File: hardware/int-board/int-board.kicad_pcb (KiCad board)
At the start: 2 copper layers, 59 x 85 mm, 25 parts, among them J1 PTSM 0,5/4-HH-2,5-THR, J2 PTSM 0,5/4-HH-2,5-THR, J3 PTSM 0,5/4-HH-2,5-THR, J4 PTSM 0,5/4-HH-2,5-THR, J5 Pi 40-pin socket, J6 GH SM07B link to EXT, J9 GPIO breakout, U1 LTV-847, U2 LTV-847, U3 LTV-847

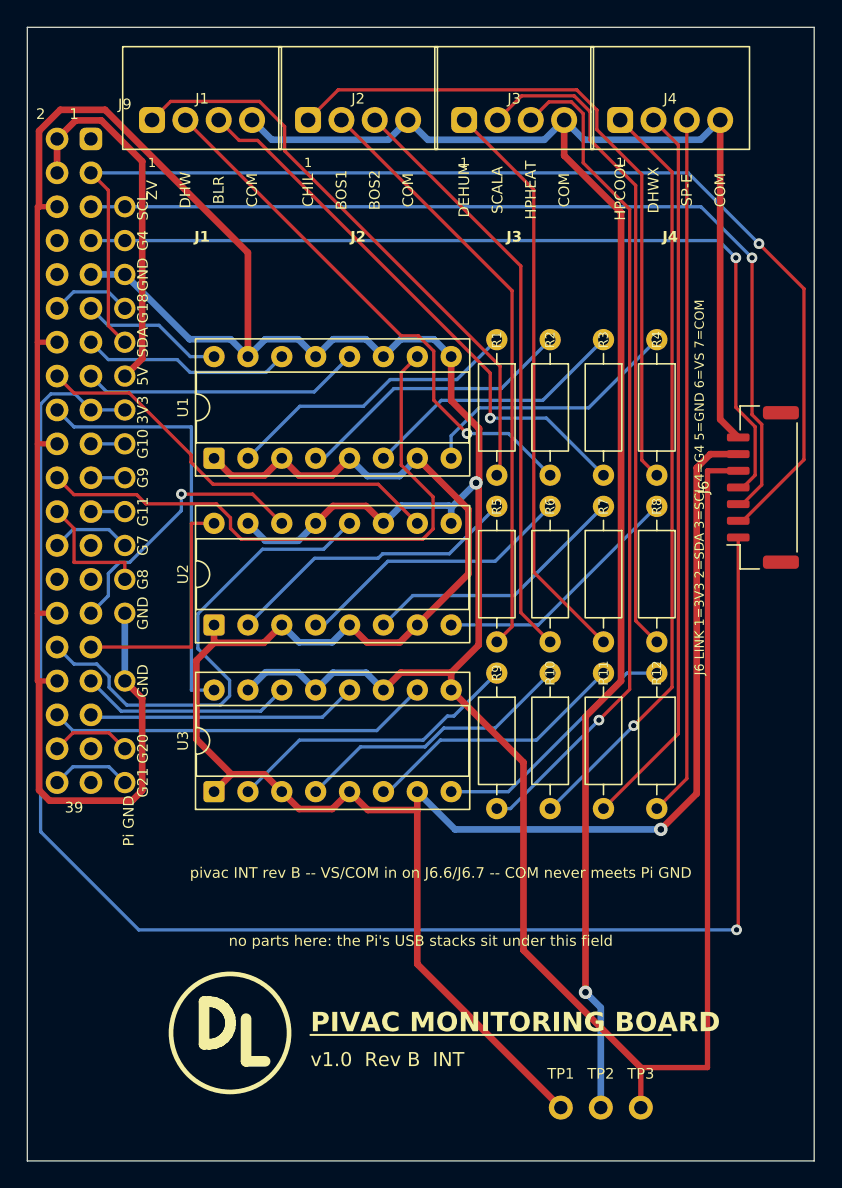
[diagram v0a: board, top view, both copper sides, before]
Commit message: Silkscreen: INT header pin numbers on their pins, J9 above its column, J5's back reference hidden; EXT probe-end labels aligned
Co-Authored-By: Claude Fable 5.1 <noreply@anthropic.com>
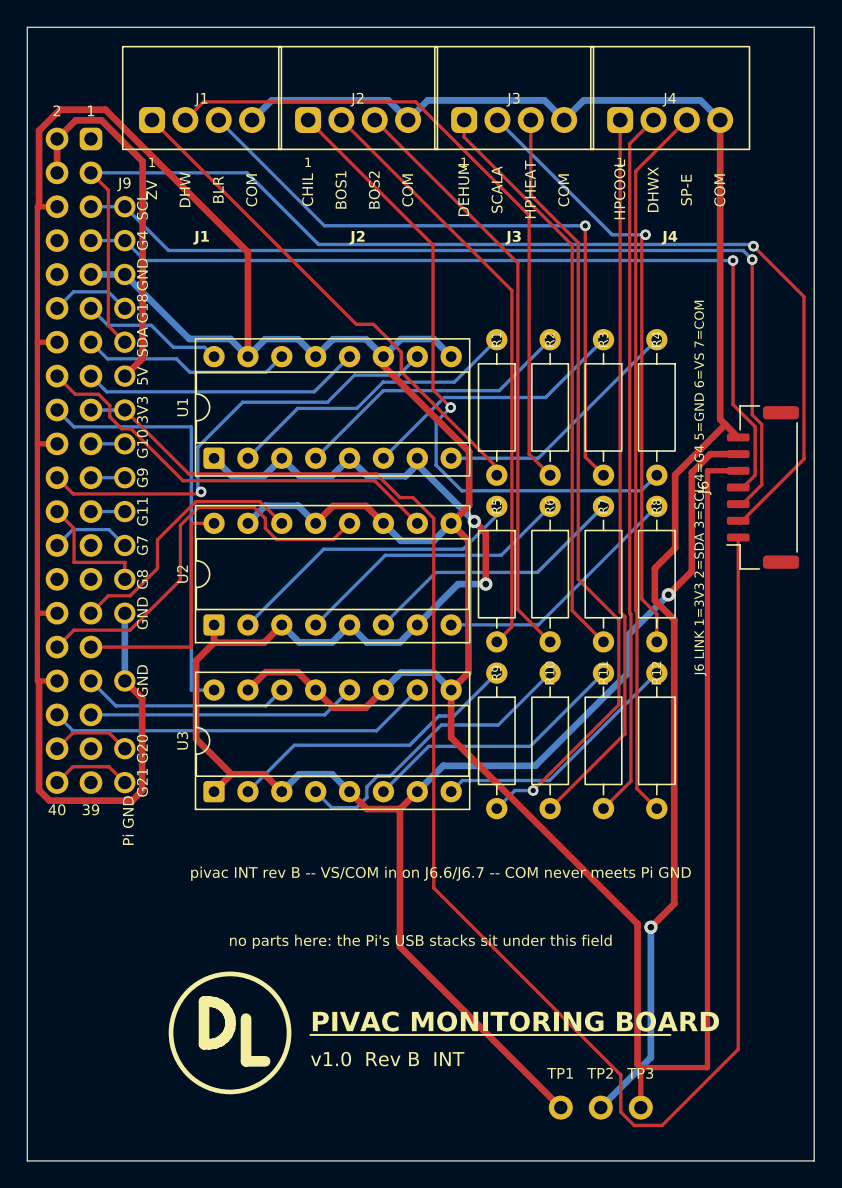
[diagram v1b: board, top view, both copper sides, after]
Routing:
- net COM: track 140.5 -> 119.4 mm
- net GPIO25: track 45.3 -> 34.1 mm, vias 0 -> 1
- net S_DHW: track 40.5 -> 50.0 mm, vias 1 -> 0
- net VS: track 162.3 -> 153.5 mm, vias 1 -> 3
- net S_BLR: track 41.9 -> 50.0 mm
- net GPIO12: track 36.8 -> 30.6 mm
- net S_ZV: track 44.2 -> 38.1 mm
- net 3V3: track 123.9 -> 129.4 mm, vias 1 -> 0
- net S_SCALA: track 50.0 -> 45.8 mm, vias 0 -> 1
- net S_HPHEAT: track 63.1 -> 59.0 mm
- net S_CHIL: track 52.5 -> 48.6 mm, vias 0 -> 1
- net S_HPCOOL: track 57.1 -> 54.1 mm, vias 1 -> 0
- net S_DHWX: track 54.7 -> 53.3 mm
- net K10: track 21.3 -> 22.7 mm
- net S_SP-E: track 52.6 -> 53.9 mm
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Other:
- board text added: "40"

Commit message: Silkscreen: J6 reference below the header, the trunk label beside H1's pin letters
Co-Authored-By: Claude Fable 5.1 <noreply@anthropic.com>
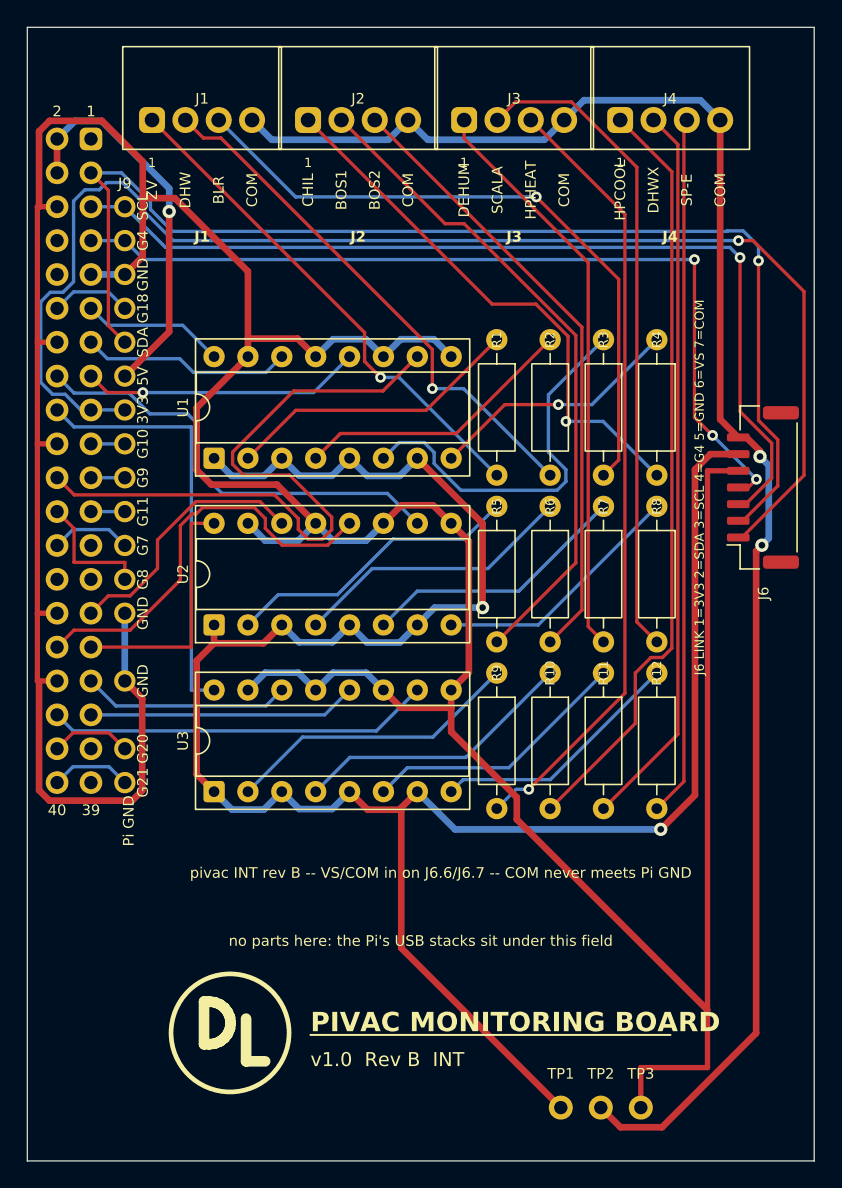
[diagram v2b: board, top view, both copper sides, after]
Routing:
- net 3V3: track 129.4 -> 102.1 mm, vias 0 -> 1
- net GPIO25: track 34.1 -> 51.0 mm, vias 1 -> 0
- net VS: track 153.5 -> 165.9 mm, vias 3 -> 2
- net S_DHW: track 50.0 -> 40.1 mm, vias 0 -> 1
- net K3: track 20.2 -> 29.3 mm
- net S_CHIL: track 48.6 -> 41.1 mm
- net COM: track 119.4 -> 124.7 mm, vias 1 -> 2
- net S_BOS1: track 44.9 -> 49.7 mm
- net GND: track 296.0 -> 292.2 mm
- net S_SCALA: track 45.8 -> 49.3 mm, vias 1 -> 0
- net S_HPCOOL: track 54.1 -> 57.5 mm
- net S_BOS2: track 44.6 -> 46.5 mm
- net +5V: track 27.5 -> 29.1 mm, vias 0 -> 1
- net GPIO23: track 32.1 -> 33.6 mm
- net K10: track 22.7 -> 21.3 mm
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
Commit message: EXT silkscreen: converter pins labelled one by one, R1's reference under R1, link legend beside J1
Co-Authored-By: Claude Fable 5.1 <noreply@anthropic.com>
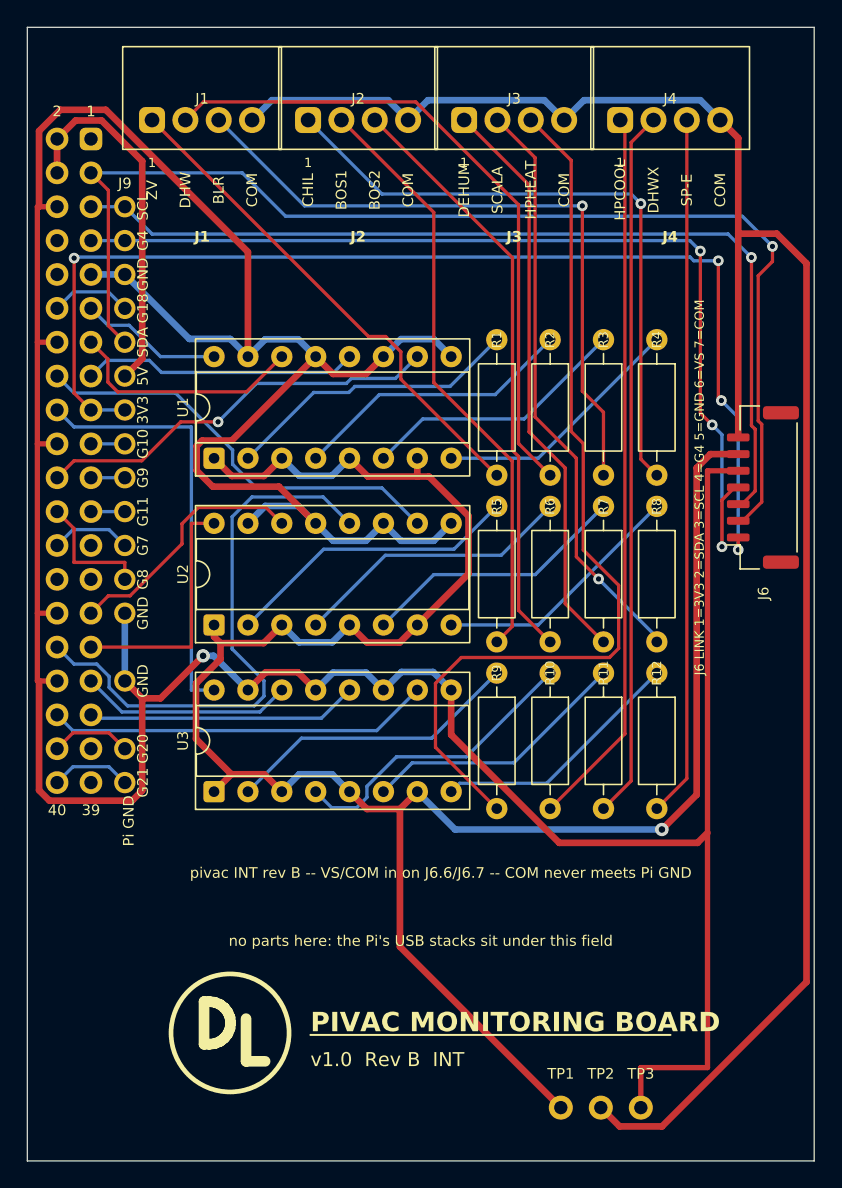
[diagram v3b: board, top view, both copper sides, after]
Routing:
- net GPIO25: track 51.0 -> 30.8 mm, vias 0 -> 1
- net COM: track 124.7 -> 143.6 mm, vias 2 -> 0
- net 3V3: track 102.1 -> 86.1 mm, vias 1 -> 4
- net GPIO12: track 30.9 -> 42.8 mm
- net S_DHW: track 40.1 -> 50.0 mm, vias 1 -> 0
- net S_HPHEAT: track 59.1 -> 68.5 mm, vias 1 -> 0
- net K3: track 29.3 -> 20.2 mm
- net GPIO4: track 65.9 -> 74.0 mm
- net S_CHIL: track 41.1 -> 48.4 mm
- net S_SCALA: track 49.3 -> 44.1 mm, vias 0 -> 1
- net S_BOS1: track 49.7 -> 44.9 mm
- net VS: track 165.9 -> 162.1 mm, vias 2 -> 1
- net S_HPCOOL: track 57.5 -> 54.1 mm
- net GPIO27: track 15.7 -> 18.0 mm
- net S_BOS2: track 46.5 -> 44.6 mm
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
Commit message: EXT silkscreen: R1 and F1 references moved clear, link legend in three lines beside J1
Co-Authored-By: Claude Fable 5.1 <noreply@anthropic.com>
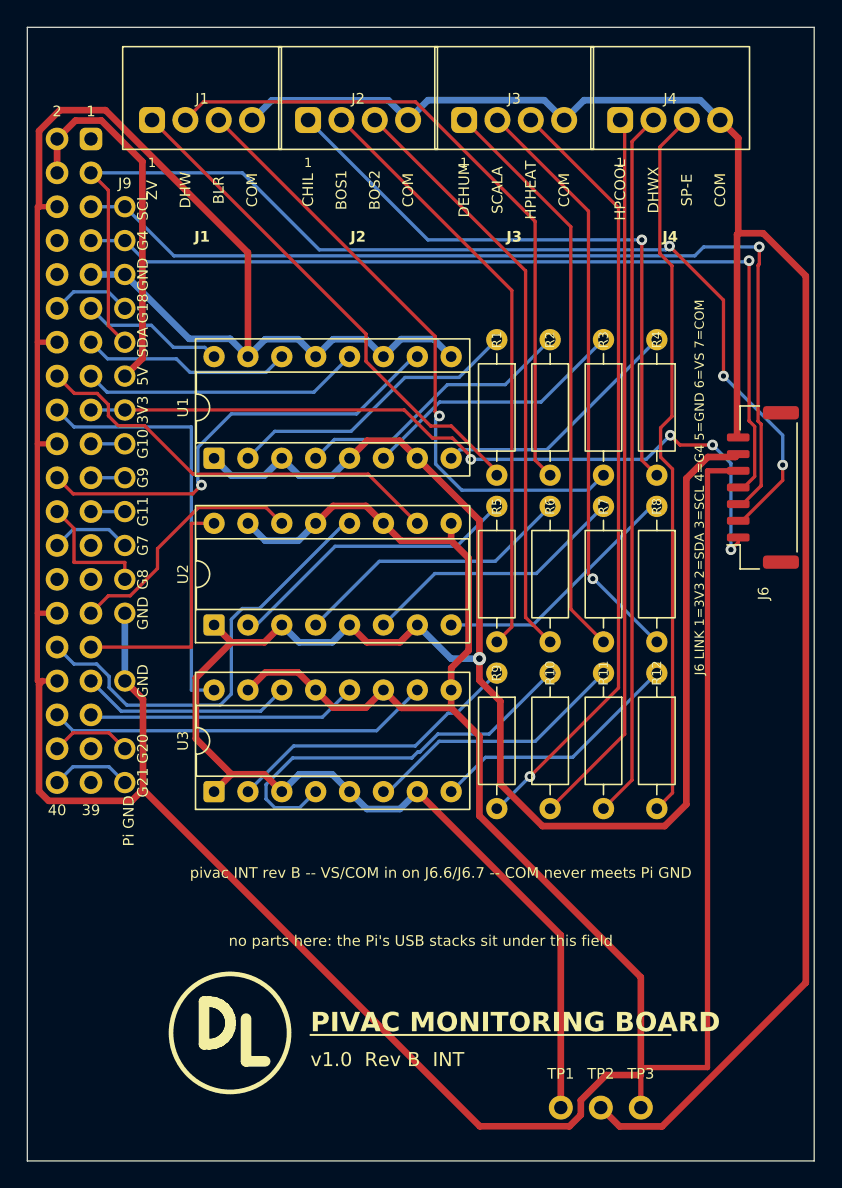
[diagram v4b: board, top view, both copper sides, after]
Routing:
- net GND: track 293.2 -> 329.4 mm, vias 1 -> 0
- net 3V3: track 86.1 -> 58.9 mm
- net VS: track 162.1 -> 173.4 mm
- net S_HPHEAT: track 68.5 -> 58.2 mm, vias 0 -> 1
- net GPIO12: track 42.8 -> 33.1 mm
- net K10: track 22.7 -> 30.3 mm
- net GPIO4: track 74.0 -> 68.0 mm, vias 3 -> 1
- net S_BLR: track 50.8 -> 46.6 mm
- net SDA: track 89.2 -> 85.3 mm, vias 1 -> 3
- net GPIO25: track 30.8 -> 33.8 mm
- net GPIO27: track 18.0 -> 15.7 mm
- net SCL: track 70.4 -> 72.2 mm
- net S_CHIL: track 48.4 -> 46.9 mm
- net S_SP-E: track 52.6 -> 54.1 mm
- net COM: track 143.6 -> 143.0 mm

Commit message: Rev B INT: 10 kΩ LED resistors in place of 12 kΩ
The resistor assortment on hand has 10 kΩ and 22 kΩ but no 12 kΩ. 10 kΩ
sets 3.4 mA per channel from the 35 V sense rail (0.11 W, under half the
1/4 W rating, far under the LTV-847's 50 mA), adds 7 mA to the bridge with
all twelve channels on, and keeps the relay contacts at a higher wetting
current. 22 kΩ would drop to about 1 mA at 21.6 VAC under the Pi's load,
half the current any build has proven.

The value appears in no gerber layer, so the ordered boards are unchanged;
the generated BOM, schematic and KiCad files are edited in place rather
than rebuilt, which would reroute the board. Rev A keeps its 12 kΩ.

Co-Authored-By: Claude Opus 5.5 <noreply@anthropic.com>
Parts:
- R1, R10, R11, R12, R2, R3, R4, R5, R6, R7, R8, R9: value 12k 1/4W -> 10k 1/4W
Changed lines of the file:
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@@
 			)
 		)
-		(property "Value" "12k 1/4W"
+		(property "Value" "10k 1/4W"
 			(at 5.08 2.37 270)
 			(layer "F.Fab")
@@
 			)
 		)
-		(property "Value" "12k 1/4W"
+		(property "Value" "10k 1/4W"
 			(at 5.08 2.37 270)
 			(layer "F.Fab")
@@
 			)
 		)
-		(property "Value" "12k 1/4W"
+		(property "Value" "10k 1/4W"
 			(at 5.08 2.37 270)
 			(layer "F.Fab")
@@
 			)
 		)
-		(property "Value" "12k 1/4W"
+		(property "Value" "10k 1/4W"
 			(at 5.08 2.37 270)
 			(layer "F.Fab")
@@
 			)
 		)
-		(property "Value" "12k 1/4W"
+		(property "Value" "10k 1/4W"
 			(at 5.08 2.37 270)
 			(layer "F.Fab")
@@
 			)
 		)
-		(property "Value" "12k 1/4W"
+		(property "Value" "10k 1/4W"
 			(at 5.08 2.37 270)
 			(layer "F.Fab")
@@
 			)
 		)
-		(property "Value" "12k 1/4W"
+		(property "Value" "10k 1/4W"
 			(at 5.08 2.37 270)
 			(layer "F.Fab")
@@
 			)
 		)
-		(property "Value" "12k 1/4W"
+		(property "Value" "10k 1/4W"
 			(at 5.08 2.37 270)
 			(layer "F.Fab")
@@
 			)
 		)
-		(property "Value" "12k 1/4W"
+		(property "Value" "10k 1/4W"
 			(at 5.08 2.37 270)
 			(layer "F.Fab")
@@
 			)
 		)
-		(property "Value" "12k 1/4W"
+		(property "Value" "10k 1/4W"
 			(at 5.08 2.37 270)
 			(layer "F.Fab")
@@
 			)
 		)
-		(property "Value" "12k 1/4W"
+		(property "Value" "10k 1/4W"
 			(at 5.08 2.37 270)
 			(layer "F.Fab")
@@
 			)
 		)
-		(property "Value" "12k 1/4W"
+		(property "Value" "10k 1/4W"
 			(at 5.08 2.37 270)
 			(layer "F.Fab")
